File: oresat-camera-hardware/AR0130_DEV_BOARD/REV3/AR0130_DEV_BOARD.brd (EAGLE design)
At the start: 40 x 44 mm, 86 parts, among them J2 4-1734592-04-1734592-0, U1 SN74AVCB164245VR, U11 KC2520B27.0000C10E00, U13 SN74AVCH8T245RHLR, U2 TPS71928-28DRVT, U3 TPS71928-28DRVT, U4 TPS71818-33DRVT, U6 MCP9808T-E/MCDFN8_2X3MC-M, U7 MCP9808T-E/MCDFN8_2X3MC-M, U9 TCA9509DGKRDGK8-M

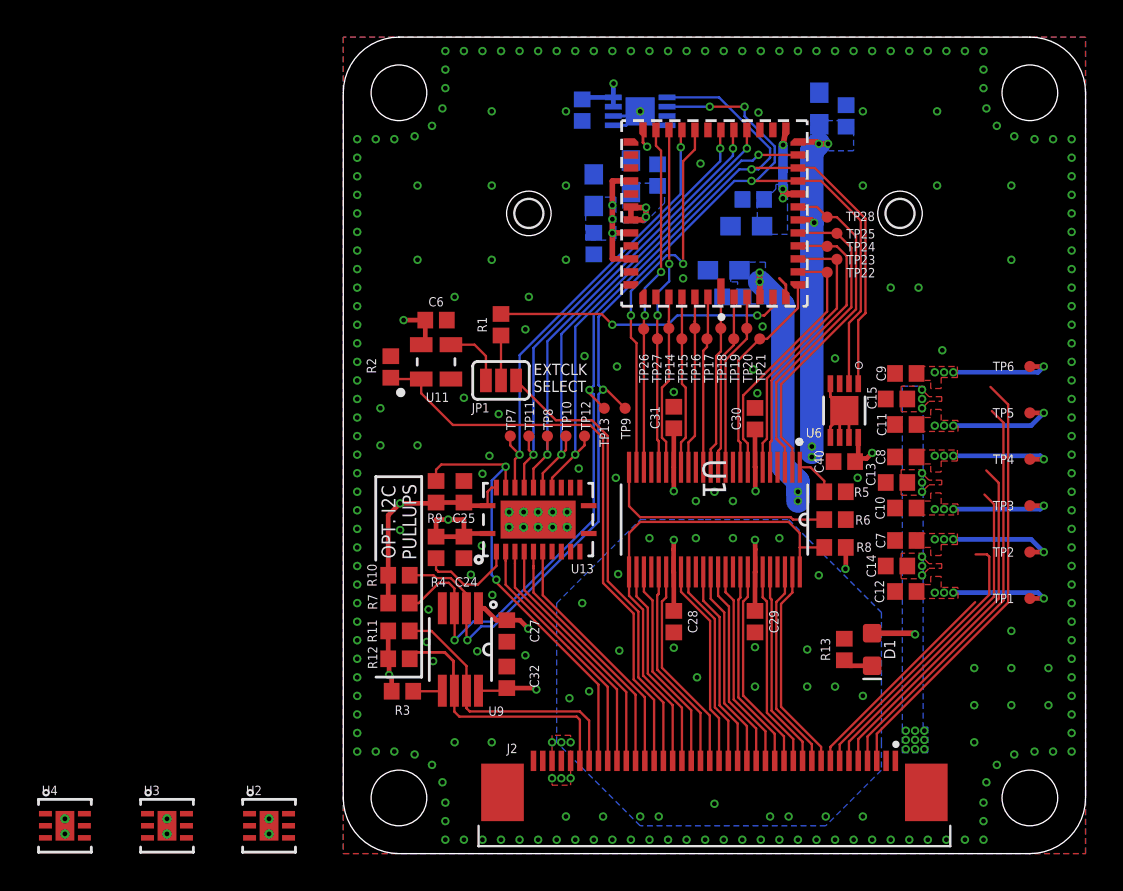
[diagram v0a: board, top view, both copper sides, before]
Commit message: addressed some camera board revisions for 3rd rev
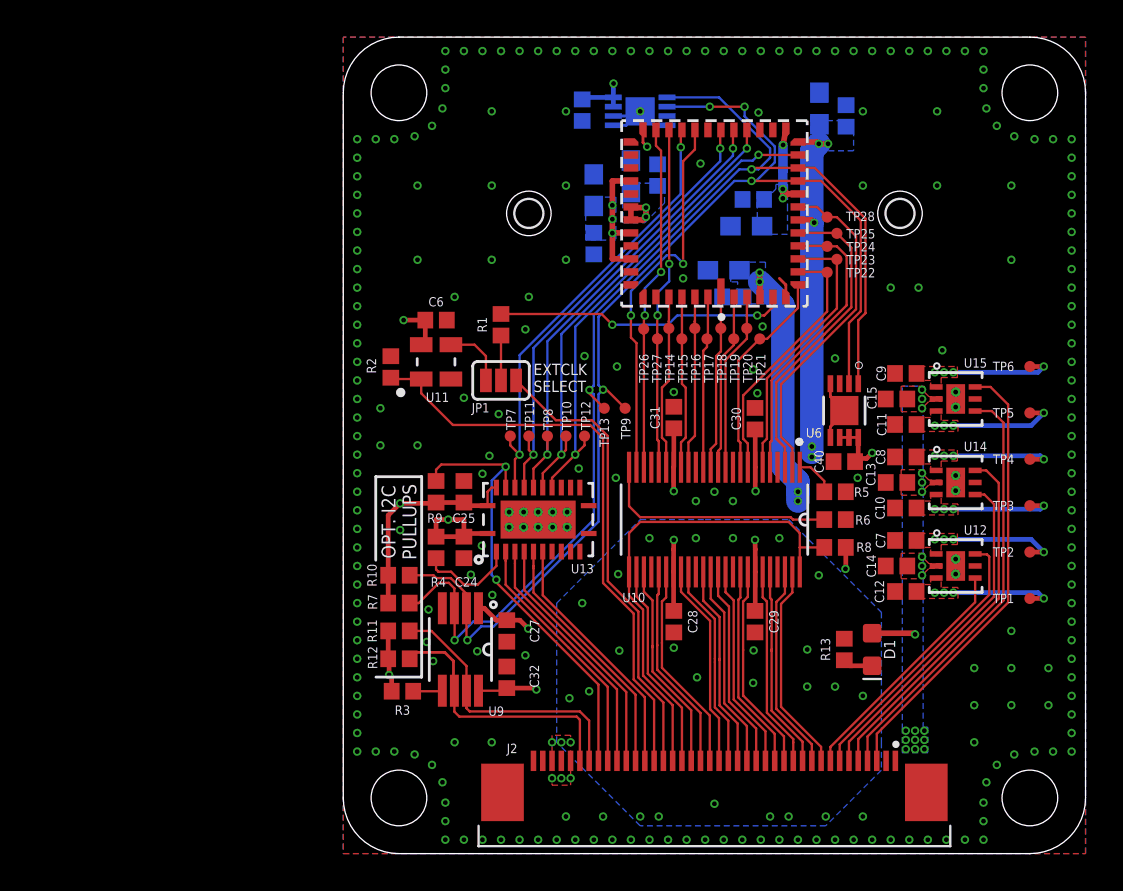
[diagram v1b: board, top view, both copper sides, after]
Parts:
- removed U2, U3: TPS71928-28DRVT, Oliver_Custom:DRV6_1P6X1
- removed U4: TPS71818-33DRVT, Oliver_Custom:DRV6_1P6X1
- added U12: TPS71818-33DRVT, Oliver_Custom:DRV6_1P6X1
- added U14, U15: TPS71928-28DRVT, Oliver_Custom:DRV6_1P6X1
- renumbered U1 to U10
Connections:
- net 1.8V: now also U12.1; no longer U4.1
- net 2.8V: now also U14.1, U6.6, U6.7; no longer U3.1
- net 3.3V: now also U12.3; no longer U4.3
- net 3.3V_EN: now also U12.4; no longer U4.4
- net 5V: now also U12.2, U14.2, U15.2; no longer U2.2, U3.2, U4.2
- net GND: now also U12.5, U12.7, U12.8, U12.9, U14.5, U14.7, U14.8, U14.9, U15.5, U15.7, U15.8, U15.9; no longer U2.5, U2.7, U2.8, U2.9, U3.5, U3.7, U3.8, U3.9, U4.5, U4.7, U4.8, U4.9, U6.6, U6.7
- net VAA_EN: now also U15.6; no longer U2.6
- net VAA_PIX_EN: now also U15.4; no longer U2.4
- net VCC: now also U15.1; no longer U2.1
- net VCC_1: now also U14.3; no longer U3.3
- net VCC_2: now also U15.3; no longer U2.3
- net VDD18_EN: now also U12.6; no longer U4.6
- net VDD_IO_EN: now also U14.6; no longer U3.6
- net VDD_PLL_EN: now also U14.4; no longer U3.4
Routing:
- net GND: track 13.3 -> 11.0 mm
- net 3.3V_EN: track 11.8 -> 13.1 mm
- net 2.8V: track 127.4 -> 128.4 mm
- net VAA_PIX_EN: track 22.1 -> 23.0 mm
- net VAA_EN: track 23.5 -> 24.3 mm
- net VDD_IO_EN: track 19.1 -> 19.7 mm
- net VDD_PLL_EN: track 17.8 -> 18.3 mm
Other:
- board text added: "AR013X-DEV-BOARD REV.3 ORESAT 2018-12-26 OLIVER REW"
- board text added: "TEMP SENSOR I2C ADDRS FRONT:0x1B BACK:0x19"
- board text removed: "AR0130-DEV-BOARD REV.2 ORESAT 2018-05-28 OLIVER REW"
